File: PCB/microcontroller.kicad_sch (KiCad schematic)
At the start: 27 parts, among them IC1 STM32F479VGT6, X1 7P-26.000MBP-T

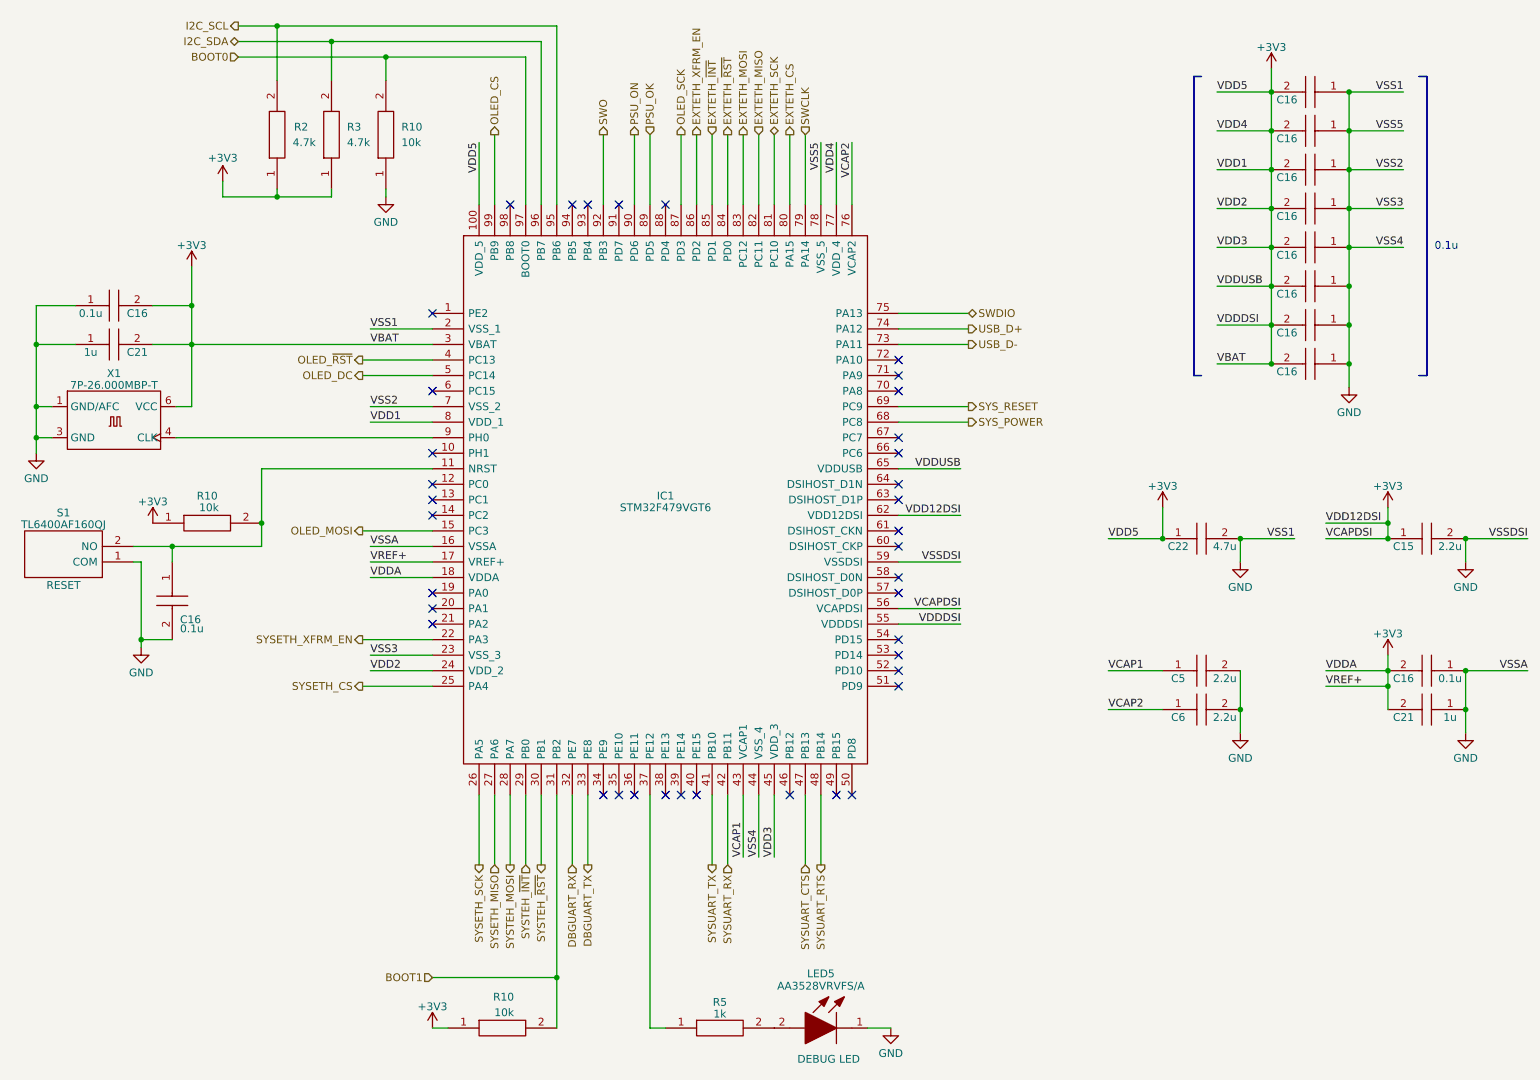
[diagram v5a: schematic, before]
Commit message: put all components behind MOSFETs (closes #39)
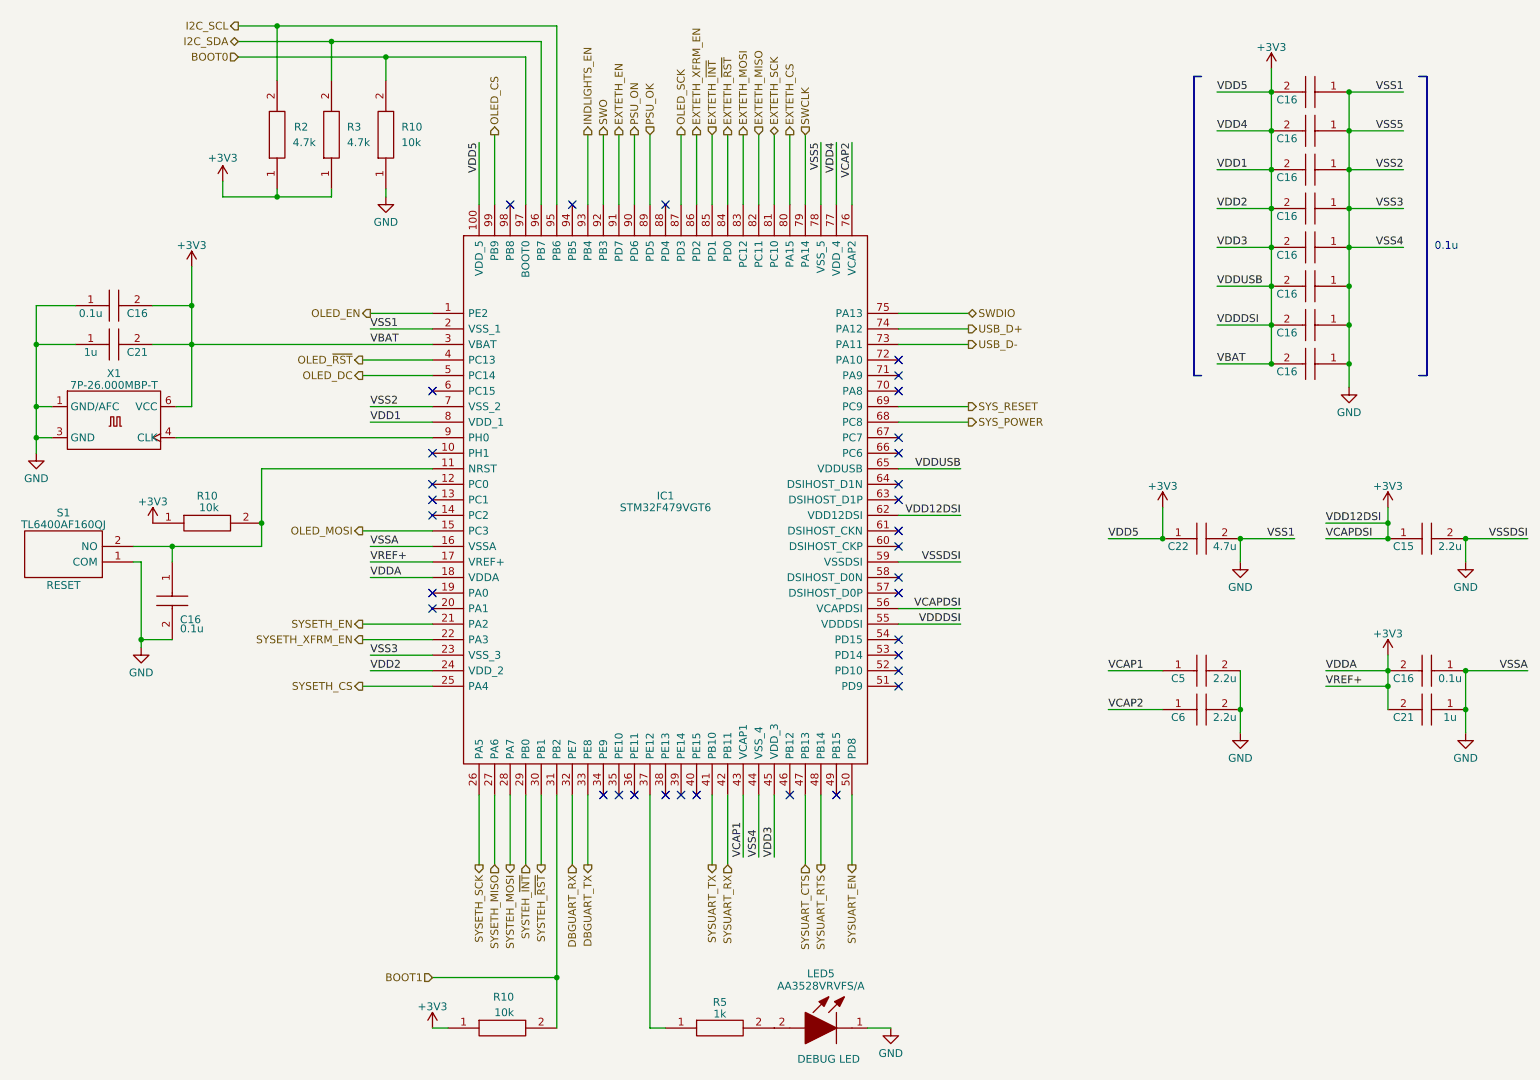
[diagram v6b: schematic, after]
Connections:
- net OLED_EN: now reaches IC1.1 (PE2)
- net SYSETH_EN: now reaches IC1.21 (PA2)
- net SYSUART_EN: now reaches IC1.50 (PD8)
- net EXTETH_EN: now reaches IC1.91 (PD7)
- net INDLIGHTS_EN: now reaches IC1.93 (PB4)
- no-connect marks 38 -> 33
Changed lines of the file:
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@@
   )
   (no_connect (at 86.36 101.6))
-  (no_connect (at 111.76 50.8))
   (no_connect (at 162.56 78.74))
   (no_connect (at 119.38 147.32))
@@
   (no_connect (at 99.06 50.8))
   (no_connect (at 86.36 114.3))
-  (no_connect (at 154.94 147.32))
   (no_connect (at 162.56 91.44))
   (no_connect (at 162.56 129.54))
@@
   (no_connect (at 86.36 96.52))
   (no_connect (at 162.56 106.68))
-  (no_connect (at 86.36 119.38))
   (no_connect (at 162.56 104.14))
-  (no_connect (at 86.36 68.58))
-  (no_connect (at 116.84 50.8))
   (no_connect (at 162.56 114.3))
   (no_connect (at 162.56 124.46))
@@
     (stroke (width 0) (type default))
   )
+  (wire (pts (xy 86.36 119.38) (xy 74.93 119.38))
+    (stroke (width 0) (type default))
+  )
   (wire (pts (xy 134.62 39.37) (xy 134.62 50.8))
     (stroke (width 0) (type default))
@@
     (stroke (width 0) (type default))
   )
+  (wire (pts (xy 111.76 39.37) (xy 111.76 50.8))
+    (stroke (width 0) (type default))
+  )
   (wire (pts (xy 43.815 106.68) (xy 58.42 106.68))
     (stroke (width 0) (type default))
@@
     (stroke (width 0) (type default))
   )
+  (wire (pts (xy 76.2 68.58) (xy 86.36 68.58))
+    (stroke (width 0) (type default))
+  )
   (wire (pts (xy 109.22 147.32) (xy 109.22 158.75))
     (stroke (width 0) (type default))
@@
     (stroke (width 0) (type default))
   )
+  (wire (pts (xy 154.94 147.32) (xy 154.94 158.75))
+    (stroke (width 0) (type default))
+  )
   (wire (pts (xy 223.52 70.485) (xy 223.52 76.835))
     (stroke (width 0) (type default))
@@
     (stroke (width 0) (type default))
   )
+  (wire (pts (xy 116.84 39.37) (xy 116.84 50.8))
+    (stroke (width 0) (type default))
+  )
   (wire (pts (xy 214.63 45.085) (xy 223.52 45.085))
     (stroke (width 0) (type default))
@@
     (effects (font (size 1.27 1.27)) (justify left))
   )
+  (hierarchical_label "INDLIGHTS_EN" (shape output) (at 111.76 39.37 90) (fields_autoplaced)
+    (effects (font (size 1.27 1.27)) (justify left))
+  )
   (hierarchical_label "SYSUART_TX" (shape output) (at 132.08 158.75 270) (fields_autoplaced)
     (effects (font (size 1.27 1.27)) (justify right))
@@
     (effects (font (size 1.27 1.27)) (justify right))
   )
+  (hierarchical_label "EXTETH_EN" (shape output) (at 116.84 39.37 90) (fields_autoplaced)
+    (effects (font (size 1.27 1.27)) (justify left))
+  )
   (hierarchical_label "DBGUART_TX" (shape output) (at 111.76 158.75 270) (fields_autoplaced)
     (effects (font (size 1.27 1.27)) (justify right))
@@
     (effects (font (size 1.27 1.27)) (justify left))
   )
+  (hierarchical_label "SYSETH_EN" (shape output) (at 74.93 119.38 180) (fields_autoplaced)
+    (effects (font (size 1.27 1.27)) (justify right))
+  )
   (hierarchical_label "SYSUART_RX" (shape input) (at 134.62 158.75 270) (fields_autoplaced)
     (effects (font (size 1.27 1.27)) (justify right))
@@
     (effects (font (size 1.27 1.27)) (justify right))
   )
+  (hierarchical_label "SYSUART_EN" (shape output) (at 154.94 158.75 270) (fields_autoplaced)
+    (effects (font (size 1.27 1.27)) (justify right))
+  )
   (hierarchical_label "SYSTEH_~{RST}" (shape output) (at 104.14 158.75 270) (fields_autoplaced)
     (effects (font (size 1.27 1.27)) (justify right))
@@
     (effects (font (size 1.27 1.27)) (justify left))
   )
+  (hierarchical_label "OLED_EN" (shape output) (at 76.2 68.58 180) (fields_autoplaced)
+    (effects (font (size 1.27 1.27)) (justify right))
+  )
   (hierarchical_label "SYS_POWER" (shape output) (at 173.99 86.36 0) (fields_autoplaced)

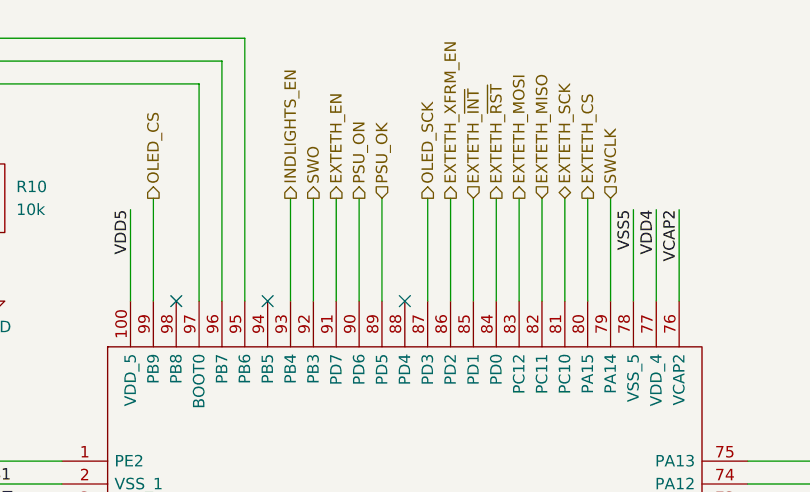
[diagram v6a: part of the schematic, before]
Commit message: eliminate power switch in lieu of direct power + sys s.b. mosfet (closes #38)
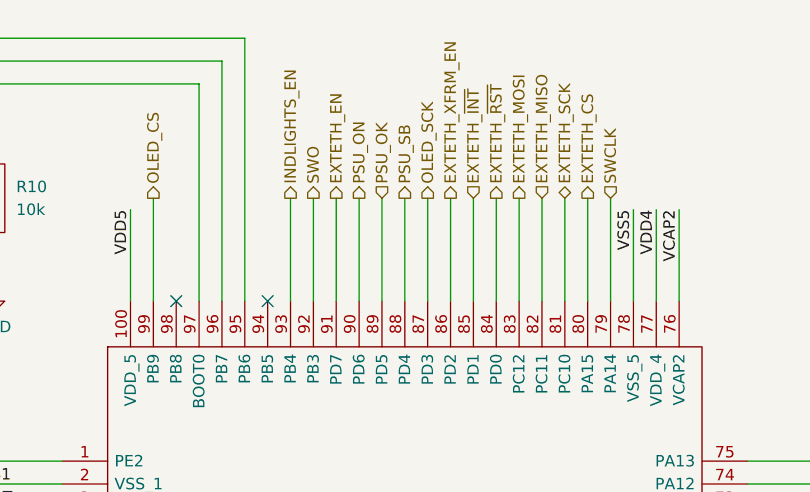
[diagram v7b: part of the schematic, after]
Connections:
- net PSU_SB: now reaches IC1.88 (PD4)
- no-connect marks 33 -> 32
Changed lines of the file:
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@@
   (no_connect (at 162.56 78.74))
   (no_connect (at 119.38 147.32))
-  (no_connect (at 124.46 50.8))
   (no_connect (at 129.54 147.32))
   (no_connect (at 99.06 50.8))
@@
     (stroke (width 0) (type default))
   )
+  (wire (pts (xy 124.46 39.37) (xy 124.46 50.8))
+    (stroke (width 0) (type default))
+  )
   (wire (pts (xy 46.99 67.31) (xy 46.99 73.66))
     (stroke (width 0) (type default))
@@
     (effects (font (size 1.27 1.27)) (justify right))
   )
+  (hierarchical_label "PSU_SB" (shape output) (at 124.46 39.37 90) (fields_autoplaced)
+    (effects (font (size 1.27 1.27)) (justify left))
+  )
   (hierarchical_label "SYS_POWER" (shape output) (at 173.99 86.36 0) (fields_autoplaced)
